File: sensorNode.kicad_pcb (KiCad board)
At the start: 2 copper layers, 0 parts

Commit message: Placed with 1206 parts
No routing attempted.
Battery is wrong.
Board outline is crude approximation of battery holder

On branch master
new file:   sensorNode.cmp
modified:   sensorNode.kicad_pcb
modified:   sensorNode.sch
new file:   sensorNode.xml
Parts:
- added BT1: 3v, Pin_Headers:Pin_Header_Straight_2x01, F.Cu at (64.0, 68.1)
- added C1: C, Capacitors_SMD:C_1210_HandSoldering, F.Cu at (80.5, 66.5)
- added P1: PIR, Pin_Headers:Pin_Header_Straight_1x04, F.Cu at (53.1, 62.5)
- added P2: PRGM, Pin_Headers:Pin_Header_Straight_1x02, F.Cu at (86.1, 79.2)
- added P3: Serial I/O, Pin_Headers:Pin_Header_Straight_1x03, F.Cu at (101.6, 79.5)
- added R1: 100, Resistors_SMD:R_1210_HandSoldering, F.Cu at (72.6, 64.0)
- added R2: 10k, Resistors_SMD:R_1210_HandSoldering, F.Cu at (80.5, 62.5)
- added R3: 10k, Resistors_SMD:R_1210_HandSoldering, F.Cu at (84.8, 74.9)
- added R4: 1k, Resistors_SMD:R_1210_HandSoldering, F.Cu at (84.8, 70.9)
- added R5: 4.7k, Resistors_SMD:R_1210_HandSoldering, F.Cu at (84.3, 54.6)
- added R6: 4.7k, Resistors_SMD:R_1210_HandSoldering, F.Cu at (60.5, 53.3)
- added R7: 4.7k, Resistors_SMD:R_1210_HandSoldering, F.Cu at (77.5, 52.8)
- added R8: 4.7k, Resistors_SMD:R_1210_HandSoldering, F.Cu at (60.5, 57.9)
- added SW1: Reset, Buttons_Switches_SMD:SW_SPST_PTS645, F.Cu at (73.2, 73.2)
- added U1: ESP-12, ESP8266:ESP-12, F.Cu at (104.1, 58.2)
- added U2: DS18B20, Housings_TO-92:TO-92_Inline_Narrow_Oval, F.Cu at (58.9, 77.2)
- added U3: ISL29035, Housings_DFN_QFN:DFN-6-1EP_2x2mm_Pitch0.5mm, F.Cu at (71.4, 57.8)
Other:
- board outline added: 55.9 x 30.5 mm

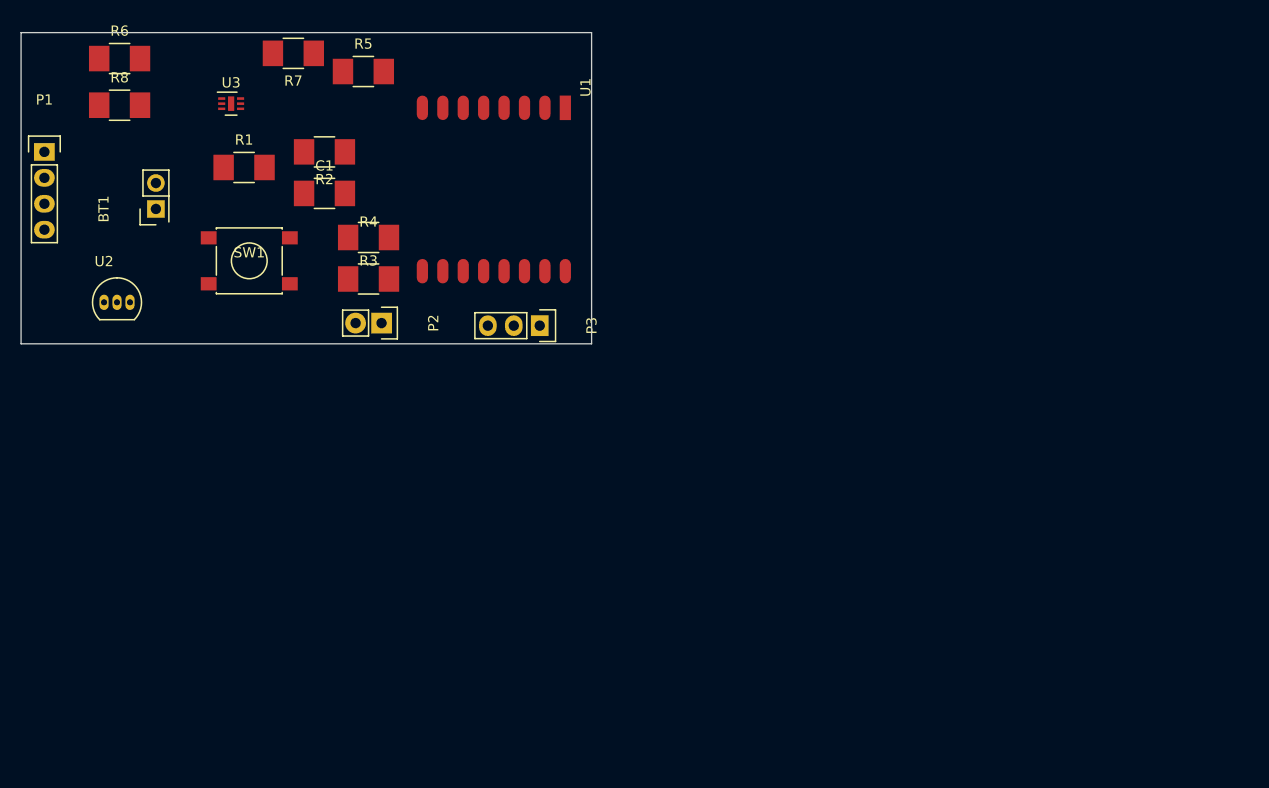
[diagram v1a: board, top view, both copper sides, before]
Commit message: Multiple changes
- Add bypass cap for isl29035
- Update footprints for battery and isl29035
- place parts on pcb
- possibly others

On branch master
new file:   fp-lib-table
modified:   sensorNode.cmp
modified:   sensorNode.kicad_pcb
modified:   sensorNode.net
modified:   sensorNode.pro
modified:   sensorNode.sch
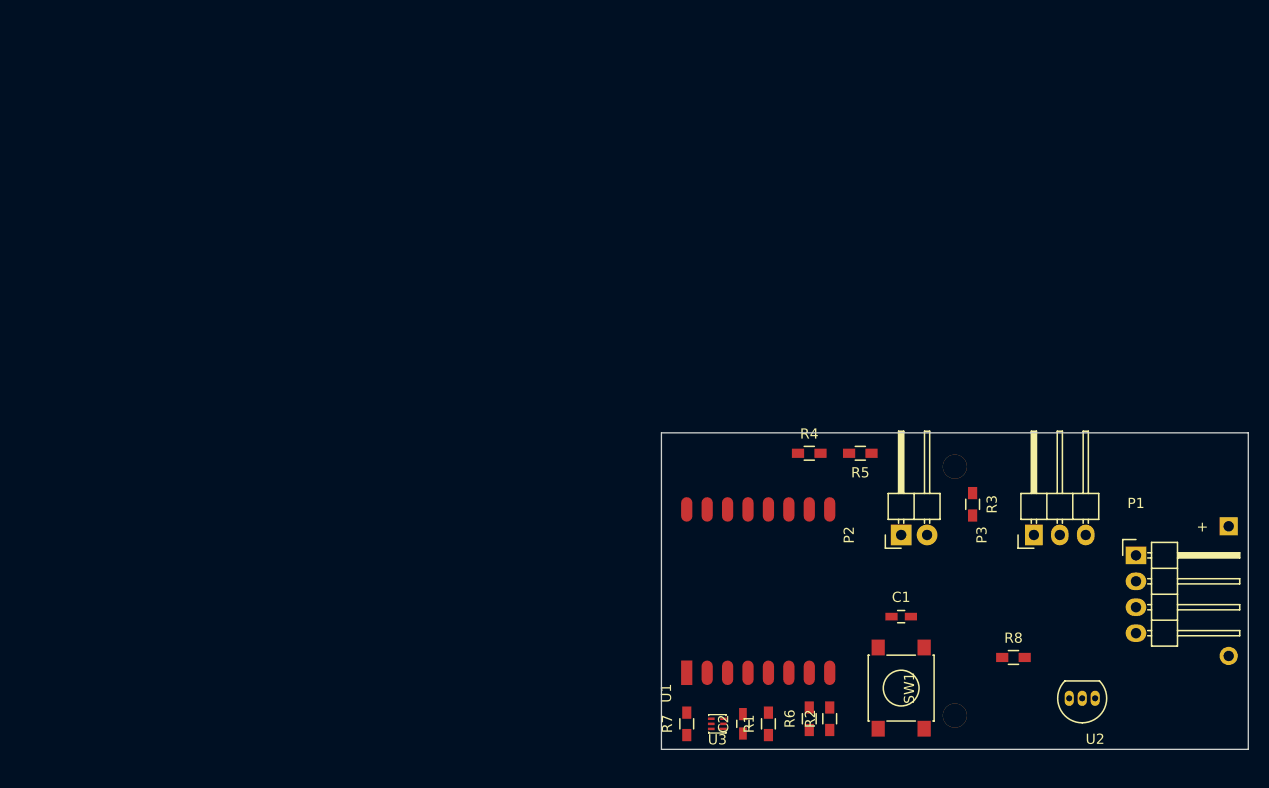
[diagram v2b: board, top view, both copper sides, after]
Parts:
- added C2: 0.1 uF, Capacitors_SMD:C_0603_HandSoldering, F.Cu at (121.5, 118.5)
- BT1: footprint Pin_Headers:Pin_Header_Straight_2x01 -> Battery_Holders:BA2AAPC; moved to B.Cu
- C1: value C -> 0.1 uF; footprint Capacitors_SMD:C_1210_HandSoldering -> Capacitors_SMD:C_0603_HandSoldering
- P1: footprint Pin_Headers:Pin_Header_Straight_1x04 -> Pin_Headers:Pin_Header_Angled_1x04
- P2: footprint Pin_Headers:Pin_Header_Straight_1x02 -> Pin_Headers:Pin_Header_Angled_1x02
- P3: footprint Pin_Headers:Pin_Header_Straight_1x03 -> Pin_Headers:Pin_Header_Angled_1x03
- R1, R2, R3, R4, R5, R6, R7, R8: footprint Resistors_SMD:R_1210_HandSoldering -> Resistors_SMD:R_0603_HandSoldering
- U3: footprint Housings_DFN_QFN:DFN-6-1EP_2x2mm_Pitch0.5mm -> sensorNode:DFN-6_1.5x1.6mm_Pitch0.5mm
- moved P1 114.0 mm to (160.0, 102.0)
- moved BT1 113.3 mm to (171.0, 105.5), turned to 0 degrees
- moved U2 104.5 mm to (156.0, 116.0), turned to 180 degrees
- moved R8 102.9 mm to (148.0, 112.0)
- moved R6 93.5 mm to (128.0, 118.0), turned to 90 degrees
- moved U3 77.2 mm to (119.0, 118.5), turned to 180 degrees
- moved SW1 76.3 mm to (137.0, 115.0), turned to 270 degrees
- moved R7 76.1 mm to (116.0, 118.5), turned to 90 degrees
- moved R1 74.9 mm to (124.0, 118.5), turned to 90 degrees
- moved R2 74.4 mm to (130.0, 118.0), turned to 90 degrees
- moved C1 70.1 mm to (137.0, 108.0)
- moved R3 63.1 mm to (144.0, 97.0), turned to 270 degrees
- moved R5 61.4 mm to (133.0, 92.0), turned to 180 degrees
- moved U1 56.6 mm to (116.0, 113.5), turned to 90 degrees
- moved P2 55.0 mm to (137.0, 100.0), turned to 90 degrees
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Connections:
- R5 pad 2: /I2C_SCL -> /I2C_SDA
- U1 pad 11: /I2C_SCL -> /I2C_SDA
- U3 pad 6: /I2C_SCL -> /I2C_SDA
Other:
- board size 55.9 x 30.5 mm -> 57.5 x 31 mm

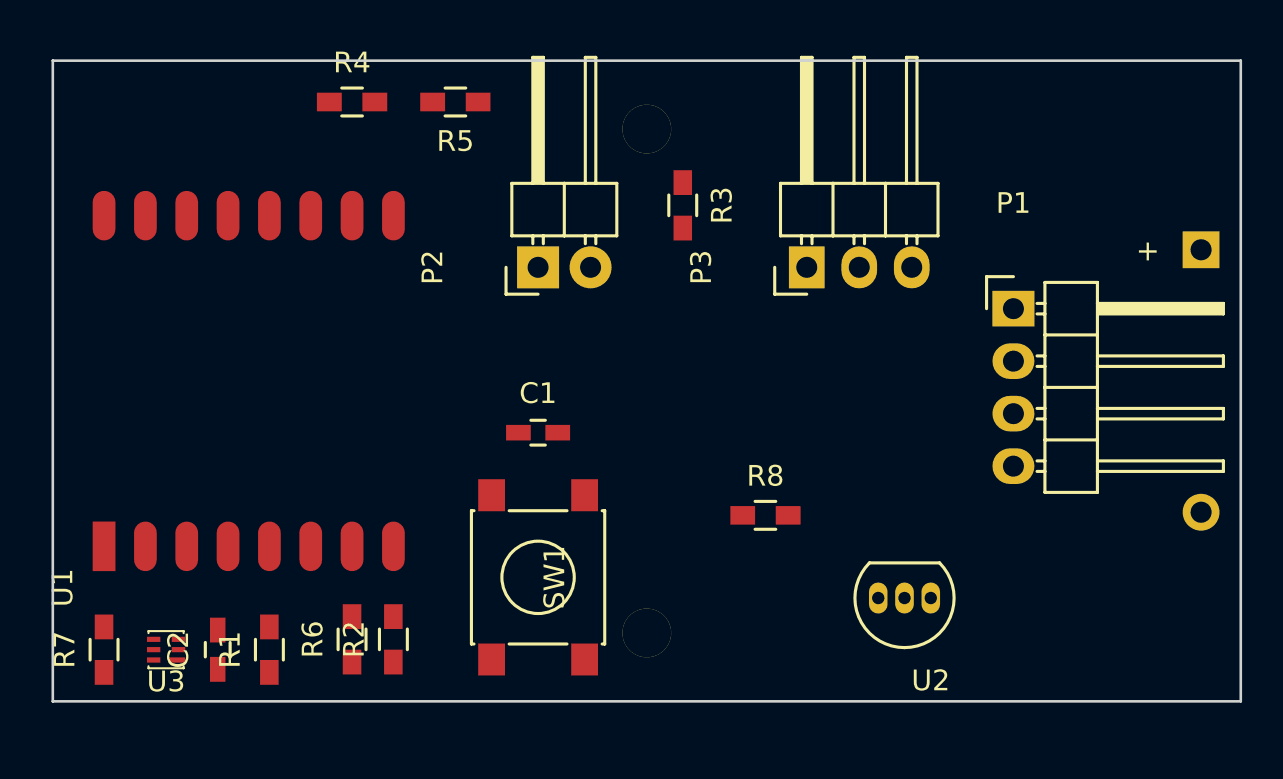
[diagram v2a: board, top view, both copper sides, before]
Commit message: Route signals and VCC
Ground plane needs to be added. Two design rule errors for U3 due
to design rule settings, not real limits.

A better switch solution would be preferred, having to connect all pins
and not being able to use common pins as jumpers made routing a lot more
difficult.

On branch master
modified:   sensorNode.kicad_pcb
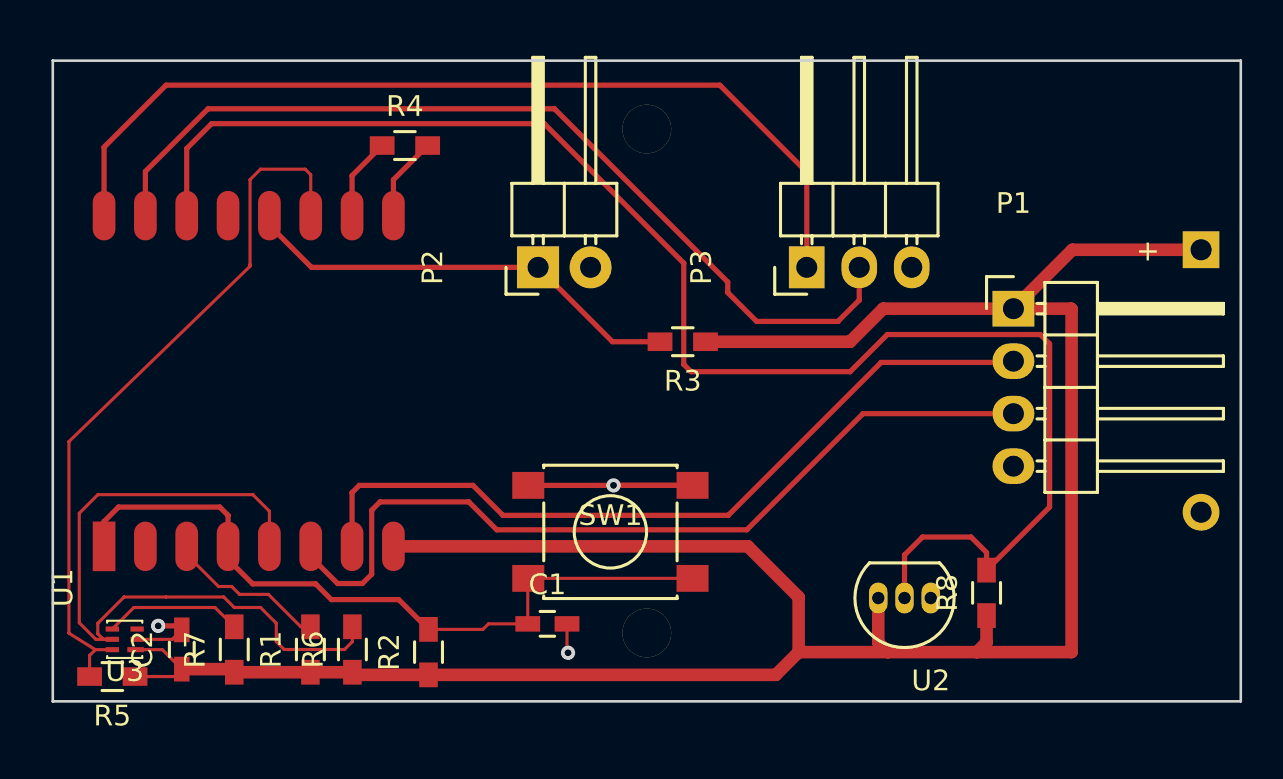
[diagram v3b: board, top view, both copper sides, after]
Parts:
- moved R5 32.4 mm to (116.4, 119.8)
- moved R8 11.3 mm to (158.7, 115.8), turned to 90 degrees
- moved C1 9.26 mm to (137.4, 117.2)
- moved R3 6.60 mm to (144.0, 103.6), turned to 180 degrees
- moved R7 6.30 mm to (122.3, 118.5)
- moved SW1 4.13 mm to (140.5, 112.8), turned to 0 degrees
- moved R4 3.31 mm to (130.6, 94.1)
- moved U3 2.06 mm to (117.0, 118.0)
- moved R1 1.98 mm to (126.0, 118.5)
- moved R2 1.81 mm to (131.7, 118.6)
- moved C2 1.74 mm to (119.8, 118.5)
- moved R6 0.49 mm to (128.0, 118.5)
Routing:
- net VCC: track 0.00 -> 122.1 mm
- net Net-(R8-Pad2): track 0.00 -> 74.1 mm
- net Net-(P3-Pad1): track 0.00 -> 44.9 mm
- net Net-(P3-Pad2): track 0.00 -> 44.5 mm
- net /PIR-Repeat: track 0.00 -> 42.0 mm
- net /PIR-Motion: track 0.00 -> 38.8 mm
- net /I2C_SCL: track 0.00 -> 38.6 mm
- net Net-(C1-Pad1): track 0.00 -> 37.9 mm
- net /I2C_SDA: track 0.00 -> 35.6 mm
- net Net-(P2-Pad1): track 0.00 -> 21.7 mm
- net GND: track 0.00 -> 20.8 mm, vias 0 -> 3
- net Net-(R1-Pad2): track 0.00 -> 7.83 mm
- net Net-(R7-Pad2): track 0.00 -> 6.72 mm
- net Net-(R4-Pad1): track 0.00 -> 4.00 mm
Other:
- net class Power added: clearance 0.254, trace_width 0.6096, via_dia 0.6858, via_drill 0.3302

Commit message: Add ground plane
Complete routing. Two design error reported due to default and VCC
design rule conflict with U3 pad spacing.

Missing 3d models for switch and ESP8320

On branch master
modified:   sensorNode.kicad_pcb
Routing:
- net GND: track 20.8 -> 32.6 mm
- added copper zone on B.Cu, net GND
